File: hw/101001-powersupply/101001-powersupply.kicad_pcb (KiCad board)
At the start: 2 copper layers, 105 x 38 mm, 85 parts, among them J101 GT-USB-7010ASV, J102 GT-USB-7010ASV, J103 2604-1102, J601 BM24-40DS, Q301 2N7002, Q302 2N7002, U201 TPS54336ADDA, U301 TPS55289RYQR, U401 ESP32-C3-MINI-1, U501 STUSB4500QTR

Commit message: Progress on board design
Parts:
- added R408: 0Ohm, Resistor_SMD:R_0402_1005Metric, F.Cu at (175.2, 110.2)
- added R409: 0Ohm, Resistor_SMD:R_0402_1005Metric, F.Cu at (176.2, 110.2)
- J102: value GT-USB-7010ASV -> GT-USB-7051A; footprint Connector_USB:USB_C_Receptacle_G-Switch_GT-USB-7010ASV -> Connector_USB:USB_C_Receptacle_G-Switch_GT-USB-7051x
- U201: footprint Package_SO:TI_SO-PowerPAD-8 -> Package_SO:TI_SO-PowerPAD-8_ThermalVias
- moved C203 15.7 mm to (155.8, 112.5), turned to 90 degrees
- moved R201 14.3 mm to (158.0, 112.5), turned to -90 degrees
- moved C204 13.9 mm to (159.0, 112.5), turned to 90 degrees
- moved R202 13.6 mm to (160.0, 112.5), turned to -90 degrees
- moved NT201 13.5 mm to (155.0, 114.5), turned to 90 degrees
- moved R203 11.7 mm to (161.5, 113.5), turned to 0 degrees
- moved J601 10.6 mm to (185.8, 114.8)
- moved C208 9.43 mm to (162.8, 115.2), turned to 180 degrees
- moved C301 8.46 mm to (160.2, 104.8)
- moved Q301 8.46 mm to (161.0, 101.8)
- moved Q302 8.46 mm to (157.5, 101.8)
- moved R301 8.46 mm to (162.2, 104.8)
- moved R302 8.46 mm to (159.2, 104.8)
- moved R303 8.46 mm to (161.2, 104.8)
- moved R304 8.46 mm to (158.2, 104.8)
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- renumbered C207 to C206, C206 to C207, R408 to R410, R409 to R411, R410 to R412, R411 to R413
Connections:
- net /External powersupply/VOUT_MEAS renamed /External powersupply/VOUT_ISN
- J601 pad 10: GND -> /Display/EXT10
- J601 pad 18: GND -> /Display/EXT18
- J601 pad 28: /Display/SCL -> GND
- J601 pad 30: GND -> /Display/SDA
- J601 pad 32: /Display/SDA -> /Display/SCL
- J601 pad 6: GND -> /Display/EXT6
- J601 pad 8: /Display/EXT8 -> GND
- U401 pad 12: /Microcontroller/VPROG_MEAS -> /Microcontroller/VSUPPLY_MEAS
- U401 pad 13: /Microcontroller/VSUPPLY_MEAS -> /Microcontroller/VPROG_MEAS
- U401 pad 20: /Display/EXT8 -> /Display/EXT12
- U401 pad 22: /Display/EXT12 -> /Display/EXT16
- U401 pad 23: /Display/EXT16 -> /Display/EXT18
- U401 pad 5: /Display/EXT4 -> /Display/EXT10
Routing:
- net GND: track 0.00 -> 108.0 mm, vias 0 -> 93
- net VPROG: track 0.00 -> 84.6 mm
- net /External powersupply/~{INT}: track 0.00 -> 74.0 mm
- net /Display/SCL: track 0.00 -> 58.5 mm, vias 0 -> 2
- net /Display/SDA: track 0.00 -> 53.4 mm, vias 0 -> 2
- net /Microcontroller/USB_PD_INT: track 0.00 -> 53.4 mm, vias 0 -> 2
- net /Microcontroller/VSUPPLY_MEAS: track 0.00 -> 46.1 mm
- net /Microcontroller/VOUT_MEAS: track 0.00 -> 42.0 mm
- net /Microcontroller/USB_PD_RESET: track 0.00 -> 40.9 mm, vias 0 -> 2
- net /External powersupply/EN_UVLO: track 0.00 -> 32.5 mm
- net /Microcontroller/VPROG_MEAS: track 0.00 -> 31.2 mm
- net VSUPPLY: track 0.00 -> 27.4 mm
- net VDD: track 0.00 -> 27.0 mm, vias 0 -> 13
- net /USB_D+: track 0.00 -> 26.1 mm
- net /USB_D-: track 0.00 -> 25.3 mm
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- added copper zone on In2.Cu, net /Interal powersupply/PH
- added copper zone on In1.Cu, net GND
- added copper zone on In3.Cu, net GND
- added copper zone on In4.Cu, net GND
- added copper zone on F.Cu, net VBUS
- added copper zone on In2.Cu, net VBUS
- added copper zone on In2.Cu, net VDD
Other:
- copper layers 2 -> 6
- board text added: "+"
- board text added: "-"
- board text added: "JLC06061H-3313 USB differential pair 0.1582mm trace width 0.2032mm trace spacing"
- board text added: "Slakkotron SRF101001R1L1"
- board text added: "sarif"

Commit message: Finalized board design
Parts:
- added C317: ~, Capacitor_SMD:C_0402_1005Metric, F.Cu at (119.8, 111.2)
- added D301: KT-0603G Emerald, LED_SMD:LED_0603_1608Metric, F.Cu at (154.0, 128.0)
- added D501: KT-0603R Red, LED_SMD:LED_0603_1608Metric, F.Cu at (155.8, 128.0)
- added G*** (x2): LOGO, LOGO, F.Cu at (104.2, 115.8)
- added Q303: 2N7002, Package_TO_SOT_SMD:SOT-23, F.Cu at (111.5, 114.8)
- added R310: 1kOhm, Resistor_SMD:R_0402_1005Metric, F.Cu at (159.2, 127.0)
- added R311: 1kOhm, Resistor_SMD:R_0402_1005Metric, F.Cu at (159.2, 128.0)
- added R505: 1kOhm, Resistor_SMD:R_0402_1005Metric, F.Cu at (159.2, 129.0)
- moved J102 8.51 mm to (200.0, 108.0), turned to 90 degrees
- moved D108 6.73 mm to (195.8, 107.2), turned to 180 degrees
- moved D107 4.61 mm to (195.8, 108.8), turned to 180 degrees
- moved C206 2.60 mm to (165.3, 117.8)
- moved C207 2.60 mm to (165.3, 120.2)
- moved C208 2.60 mm to (165.3, 115.2)
- moved C201 2.50 mm to (160.8, 124.2)
- moved C202 2.50 mm to (160.0, 122.8)
- moved C203 2.50 mm to (158.2, 112.5)
- moved C204 2.50 mm to (161.5, 112.5)
- moved C205 2.50 mm to (158.5, 122.2)
- moved D109 2.50 mm to (195.8, 110.2), turned to 180 degrees
- moved L201 2.50 mm to (166.0, 124.8)
- moved NT201 2.50 mm to (157.5, 114.5)
- moved R201 2.50 mm to (160.5, 112.5)
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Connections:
- net /Interal powersupply/AGND renamed /Internal powersupply/AGND
- net /Interal powersupply/BOOT renamed /Internal powersupply/BOOT
- net /Interal powersupply/COMP renamed /Internal powersupply/COMP
- net /Interal powersupply/PH renamed /Internal powersupply/PH
- net /Interal powersupply/SS renamed /Internal powersupply/SS
- net /Interal powersupply/VSENSE renamed /Internal powersupply/VSENSE
- U501 pad 15: unconnected-(U501-GPIO-Pad15) -> /USB PD Controller/LED_OD
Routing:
- net VPROG: track 84.6 -> 20.8 mm, vias 0 -> 6
- net GND: track 108.0 -> 164.7 mm, vias 93 -> 135
- net /External powersupply/LED_OD: track 0.00 -> 52.9 mm
- net /External powersupply/VOUT_DIRECT: track 0.00 -> 46.1 mm
- net /Display/SDA: track 53.4 -> 85.7 mm, vias 2 -> 3
- net /Microcontroller/VOUT_MEAS: track 42.0 -> 73.4 mm
- net /Display/SCL: track 58.5 -> 89.4 mm, vias 2 -> 3
- net VBUS: track 9.66 -> 37.1 mm, vias 11 -> 23
- net /USB PD Controller/LED_OD: track 0.00 -> 24.2 mm
- net /External powersupply/VOUT_ISN: track 0.00 -> 19.8 mm
- net /External powersupply/AGND: track 0.00 -> 17.3 mm, vias 0 -> 2
- net VOUT: track 0.00 -> 17.1 mm
- net /External powersupply/SW2: track 0.00 -> 8.75 mm
- net /External powersupply/SW1: track 0.00 -> 8.75 mm
- net /USB_D+: track 26.1 -> 18.2 mm
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- added copper zone on F.Cu, net VOUT
- added copper zone on In2.Cu, net VPROG
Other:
- board text added: "ENABLED"
- board text added: "JLCJLCJLCJLC"
- board text added: "POWER"
- board text added: "PROG"
- board text added: "SHORT"

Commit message: Fixed Ccomp
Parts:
- added C209: 22nF 50V X7R, Capacitor_SMD:C_0402_1005Metric, F.Cu at (160.8, 112.0)
- moved C204 2.25 mm to (159.2, 112.5)
- moved R201 0.56 mm to (160.8, 113.0), turned to 180 degrees
- moved R202 0.25 mm to (162.2, 112.5)
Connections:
- R201 pad 1: /Internal powersupply/AGND -> /Internal powersupply/COMP2
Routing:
- net /Internal powersupply/COMP: track 2.63 -> 3.88 mm
- net /Internal powersupply/COMP2: track 0.00 -> 1.01 mm
- net /Internal powersupply/AGND: track 6.74 -> 7.24 mm
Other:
- board text added: "Slakkotron SRF101001R2L1"
- board text removed: "Slakkotron SRF101001R1L1"

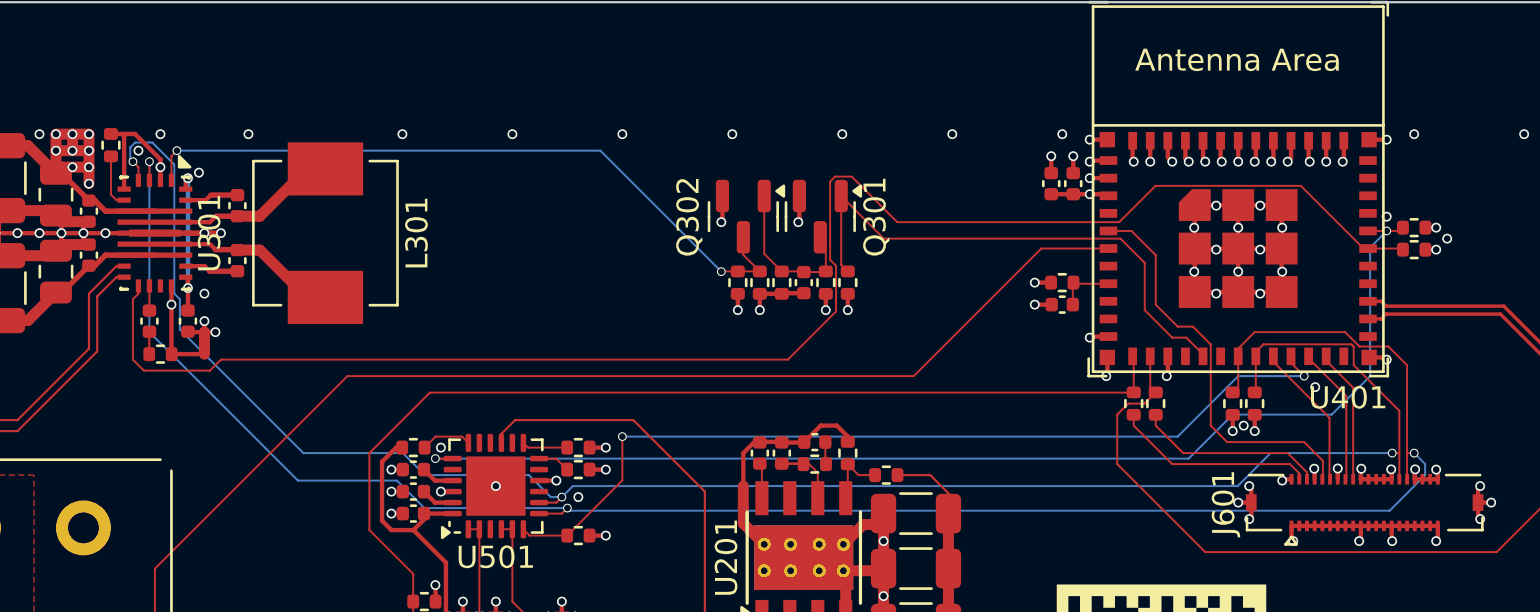
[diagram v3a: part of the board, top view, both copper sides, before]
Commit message: Added strapping pins bias and buttons
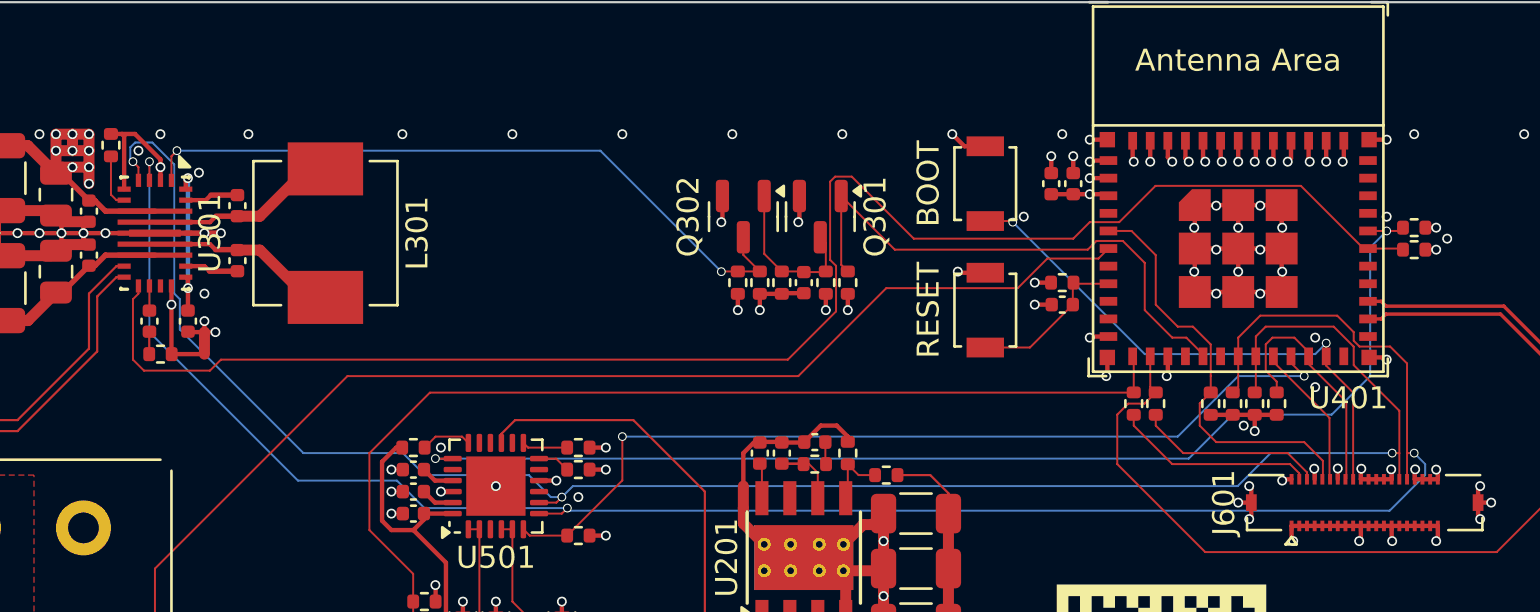
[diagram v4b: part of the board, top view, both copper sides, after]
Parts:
- added R414: 10kOhm, Resistor_SMD:R_0402_1005Metric, F.Cu at (178.8, 110.2)
- added R415: 10kOhm, Resistor_SMD:R_0402_1005Metric, F.Cu at (181.8, 110.2)
- added SW401: B3U-1000P, Button_Switch_SMD:SW_SPST_B3U-1000P, F.Cu at (168.5, 106.0)
- added SW402: B3U-1000P, Button_Switch_SMD:SW_SPST_B3U-1000P, F.Cu at (168.5, 100.2)
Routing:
- net /Display/EXT18: track 6.10 -> 24.9 mm, vias 0 -> 2
- net /Display/EXT16: track 6.32 -> 11.3 mm
- net /Microcontroller/EN: track 2.62 -> 7.41 mm
- net GND: track 164.7 -> 167.7 mm, vias 135 -> 138
- net VDD: track 29.6 -> 31.8 mm, vias 14 -> 13
- net /Display/SCL: track 89.4 -> 90.6 mm
- net /Display/SDA: track 85.7 -> 86.8 mm
- net /Display/EXT10: track 18.4 -> 19.1 mm
- net /External powersupply/~{INT}: track 71.6 -> 72.3 mm
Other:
- board text added: "BOOT"
- board text added: "RESET"

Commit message: Hardware improvements
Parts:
- added R101: 1kOhm, Resistor_SMD:R_0402_1005Metric, F.Cu at (140.8, 121.8)
- added R102: 1kOhm, Resistor_SMD:R_0402_1005Metric, F.Cu at (157.8, 126.5)
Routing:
- net GND: track 167.7 -> 169.4 mm, vias 138 -> 139
- net VSUPPLY: track 27.4 -> 28.1 mm
- net VPROG: track 20.8 -> 21.3 mm, vias 6 -> 7
